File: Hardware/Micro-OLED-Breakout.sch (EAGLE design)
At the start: 23 parts

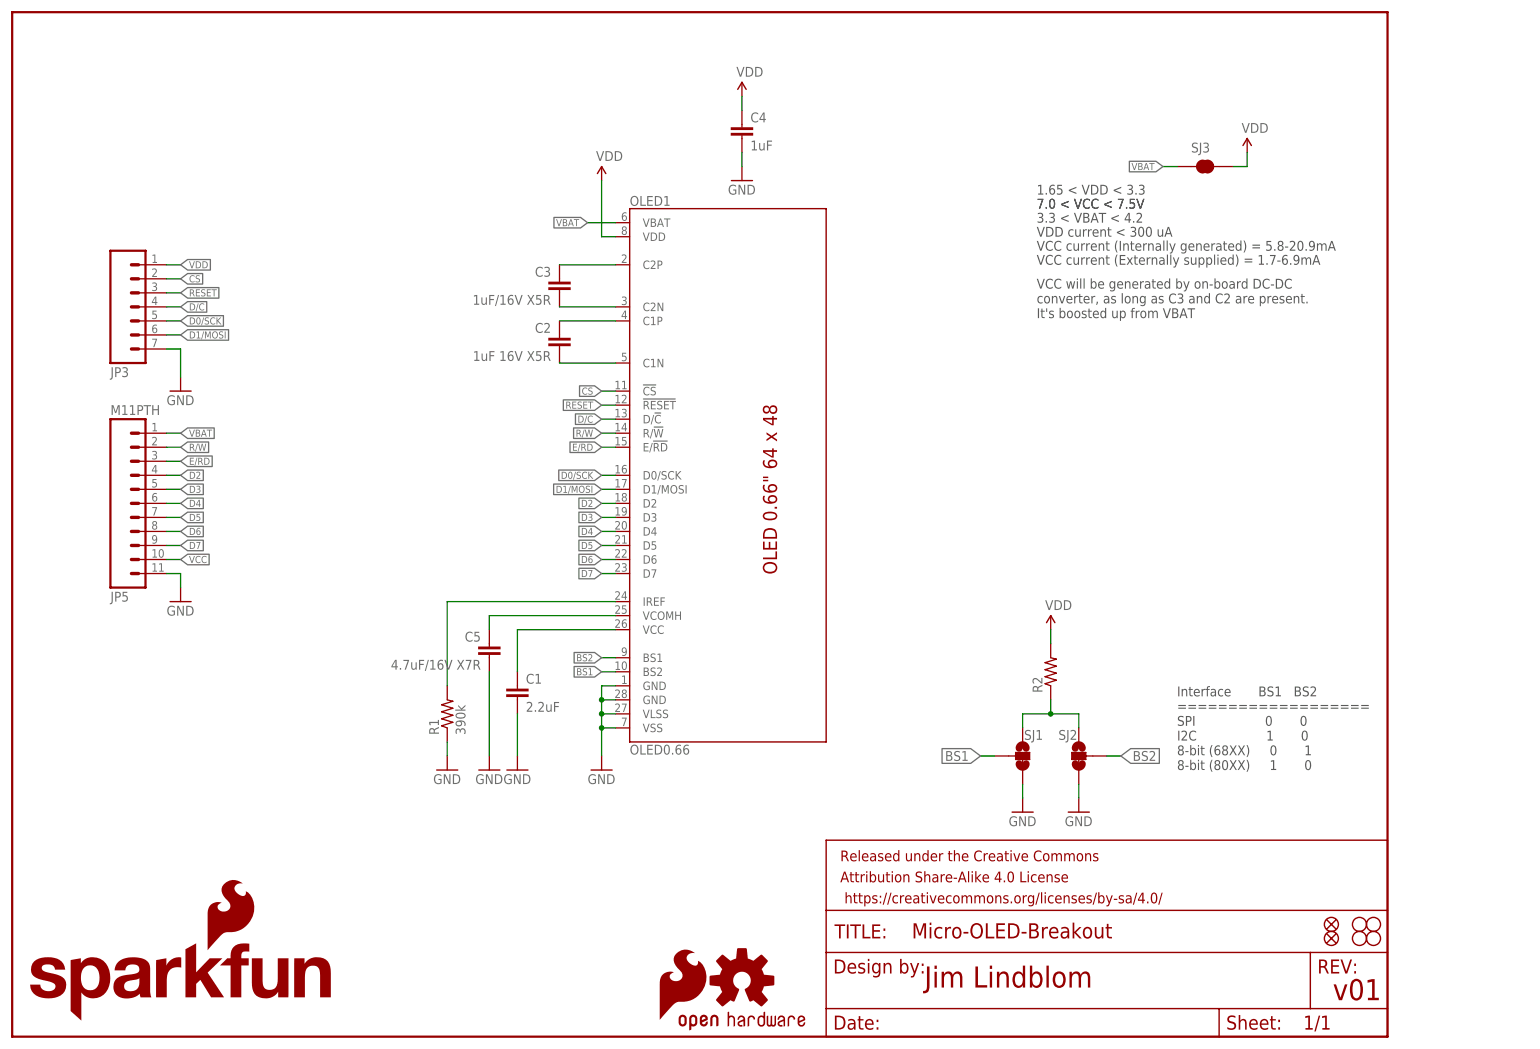
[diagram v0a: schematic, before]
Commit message: Revising board shape, OLED (v02)
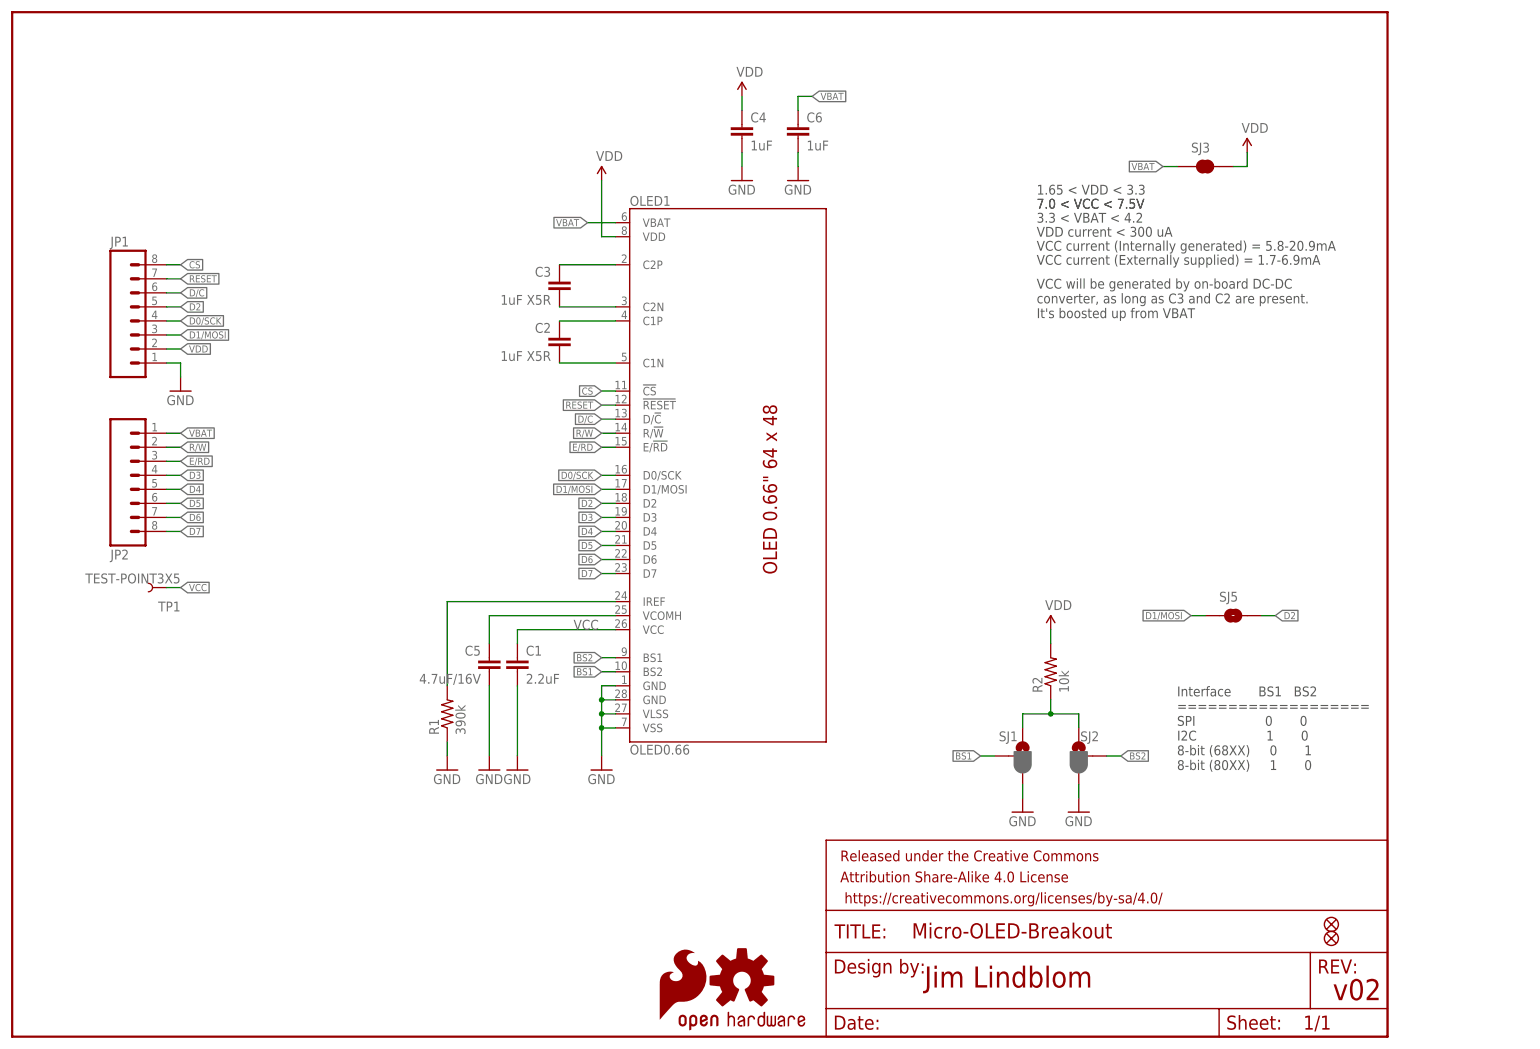
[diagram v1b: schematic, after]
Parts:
- removed JP3: (no value), SparkFun-Connectors:M07
- removed JP5: M11PTH, SparkFun-Connectors:M11PTH
- removed LOGO1: OSHW-LOGOS, SparkFun-Aesthetics:OSHW-LOGOS
- removed STANDOFF1, STANDOFF2, STANDOFF3, STANDOFF4: STAND-OFF, SparkFun-Electromechanical:STAND-OFF
- added C6: 1uF, SparkFun-Passives:CAP0603-CAP
- added JP1, JP2: (no value), SparkFun-Connectors:M08
- added SJ5: JUMPER-PAD-2-NOYES_SILK, SparkFun-Passives:JUMPER-PAD-2-NOYES_SILK
- added TP1: TEST-POINT3X5, SparkFun-Passives:TEST-POINT3X5
- C1: device SparkFun-Passives:CAP0603-CAP -> SparkFun-Passives:CAP0805
- C2: value 1uF 16V X5R -> 1uF X5R; device SparkFun-Passives:CAP0603-CAP -> SparkFun-Passives:CAP0805
- C3: value 1uF/16V X5R -> 1uF X5R; device SparkFun-Passives:CAP0603-CAP -> SparkFun-Passives:CAP0805
- C5: value 4.7uF/16V X7R -> 4.7uF/16V; device SparkFun-Passives:CAP0603-CAP -> SparkFun-Passives:CAP1206
- LOGO3: value SFE_LOGO_NAME_FLAME.1_INCH -> OSHW-LOGOS; device SparkFun-Aesthetics:SFE_LOGO_NAME_FLAME.1_INCH -> SparkFun-Aesthetics:OSHW-LOGOS
- R2: value (none) -> 10k
- SJ1: value JUMPER-PAD-3-2OF3_NC_BY_TRACE -> BS1; device SparkFun-Passives:JUMPER-PAD-3-2OF3_NC_BY_TRACE -> SparkFun-Passives:JUMPER-PAD-3-2OF3_NC_BY_PASTE
- SJ2: value JUMPER-PAD-3-2OF3_NC_BY_TRACE -> BS2; device SparkFun-Passives:JUMPER-PAD-3-2OF3_NC_BY_TRACE -> SparkFun-Passives:JUMPER-PAD-3-2OF3_NC_BY_PASTE
- SJ3: value JUMPER-PAD-2-NC_BY_TRACE -> JUMPER-PAD-2-NC_BY_TRACENO_SILK; device SparkFun-Passives:JUMPER-PAD-2-NC_BY_TRACE -> SparkFun-Passives:JUMPER-PAD-2-NC_BY_TRACENO_SILK
- renumbered LOGO2 to LOGO4
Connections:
- net CS: now also JP1.8; no longer JP3.2
- net D/C: now also JP1.6; no longer JP3.4
- net D0/SCK: now also JP1.4; no longer JP3.5
- net D1/MOSI: now also JP1.3, SJ5.1; no longer JP3.6
- net D2: now also JP1.5, SJ5.2; no longer JP5.4
- net D3: now also JP2.4; no longer JP5.5
- net D4: now also JP2.5; no longer JP5.6
- net D5: now also JP2.6; no longer JP5.7
- net D6: now also JP2.7; no longer JP5.8
- net D7: now also JP2.8; no longer JP5.9
- net E/RD: now also JP2.3; no longer JP5.3
- net GND: now also C6.2, JP1.1; no longer JP3.7, JP5.11
- net R/W: now also JP2.2; no longer JP5.2
- net RESET: now also JP1.7; no longer JP3.3
- net VBAT: now also C6.1, JP2.1; no longer JP5.1
- net VCC: now also TP1.1; no longer JP5.10
- net VDD: now also JP1.2; no longer JP3.1
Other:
- note added: "v02"
- note removed: "v01"
- moved on the sheet: C1, C5

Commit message: Fixing swapped BS1 and BS2 labels (v03)
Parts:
- added TP2: TEST-POINT3X5, SparkFun-Passives:TEST-POINT3X5
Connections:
- net BS1: now also OLED1.BS1; no longer OLED1.BS2
- net BS2: now also OLED1.BS2; no longer OLED1.BS1
- net VCC: now also TP2.1
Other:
- note added: "v03"
- note removed: "v02"

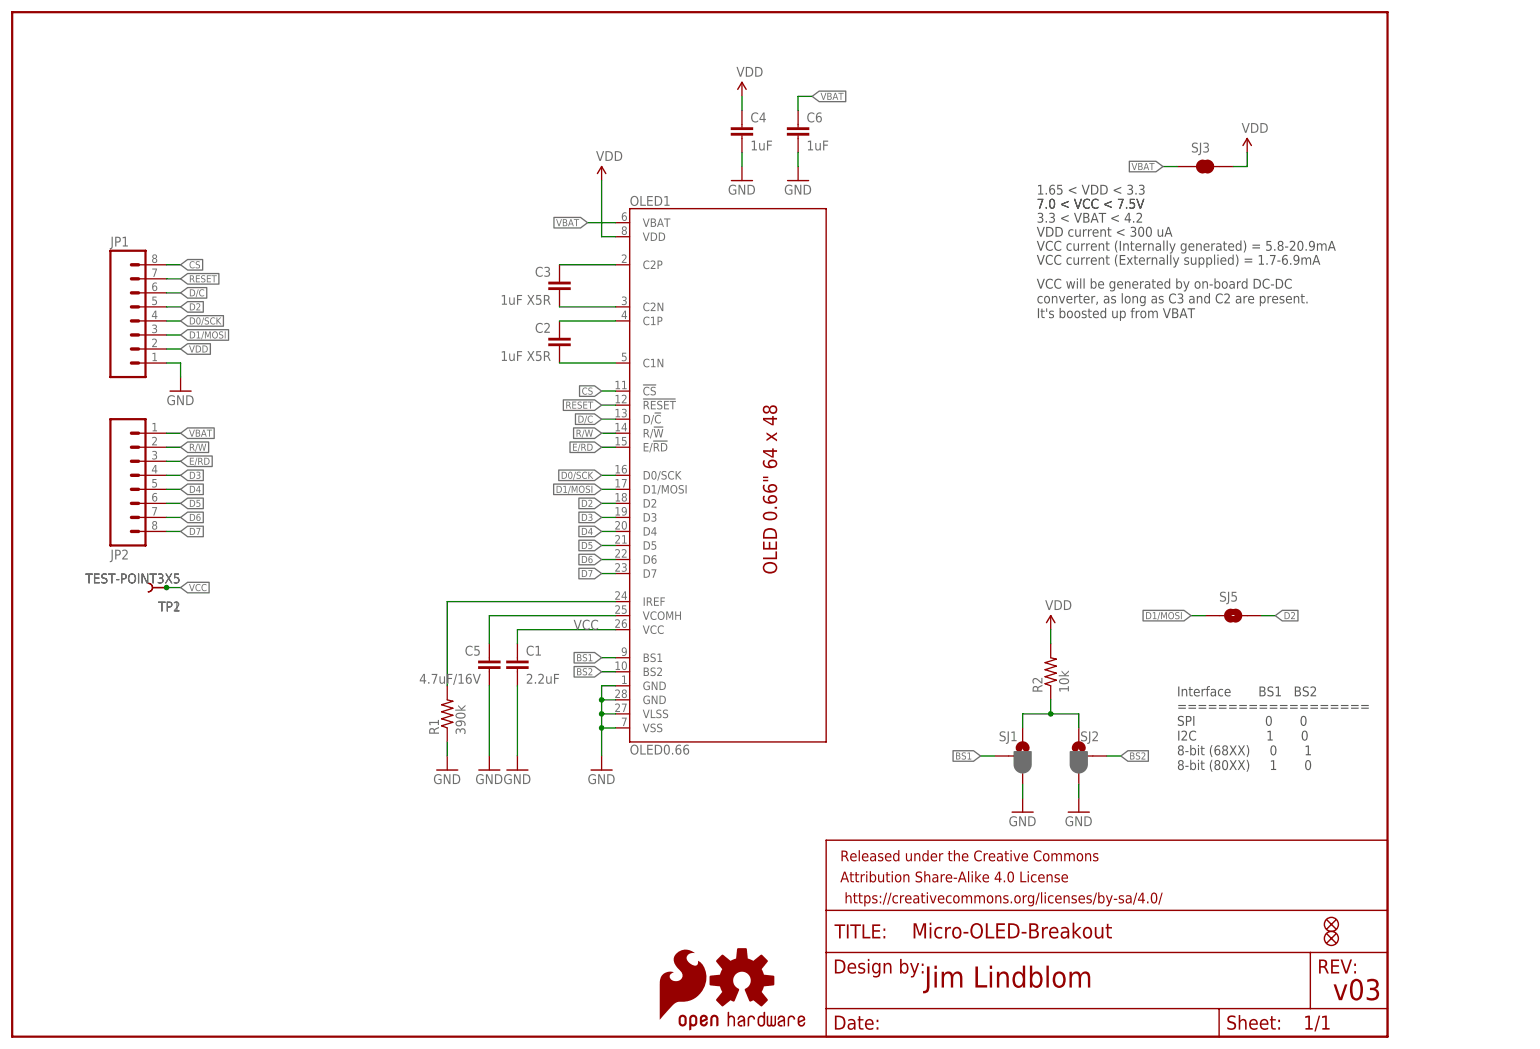
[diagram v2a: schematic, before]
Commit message: Adding D/C jumper (open by default) (v04)
Allows address selection in I2C mode.

Also:
* adding some notes to schematic
* Shuffling around silk labels. Avoiding holes.
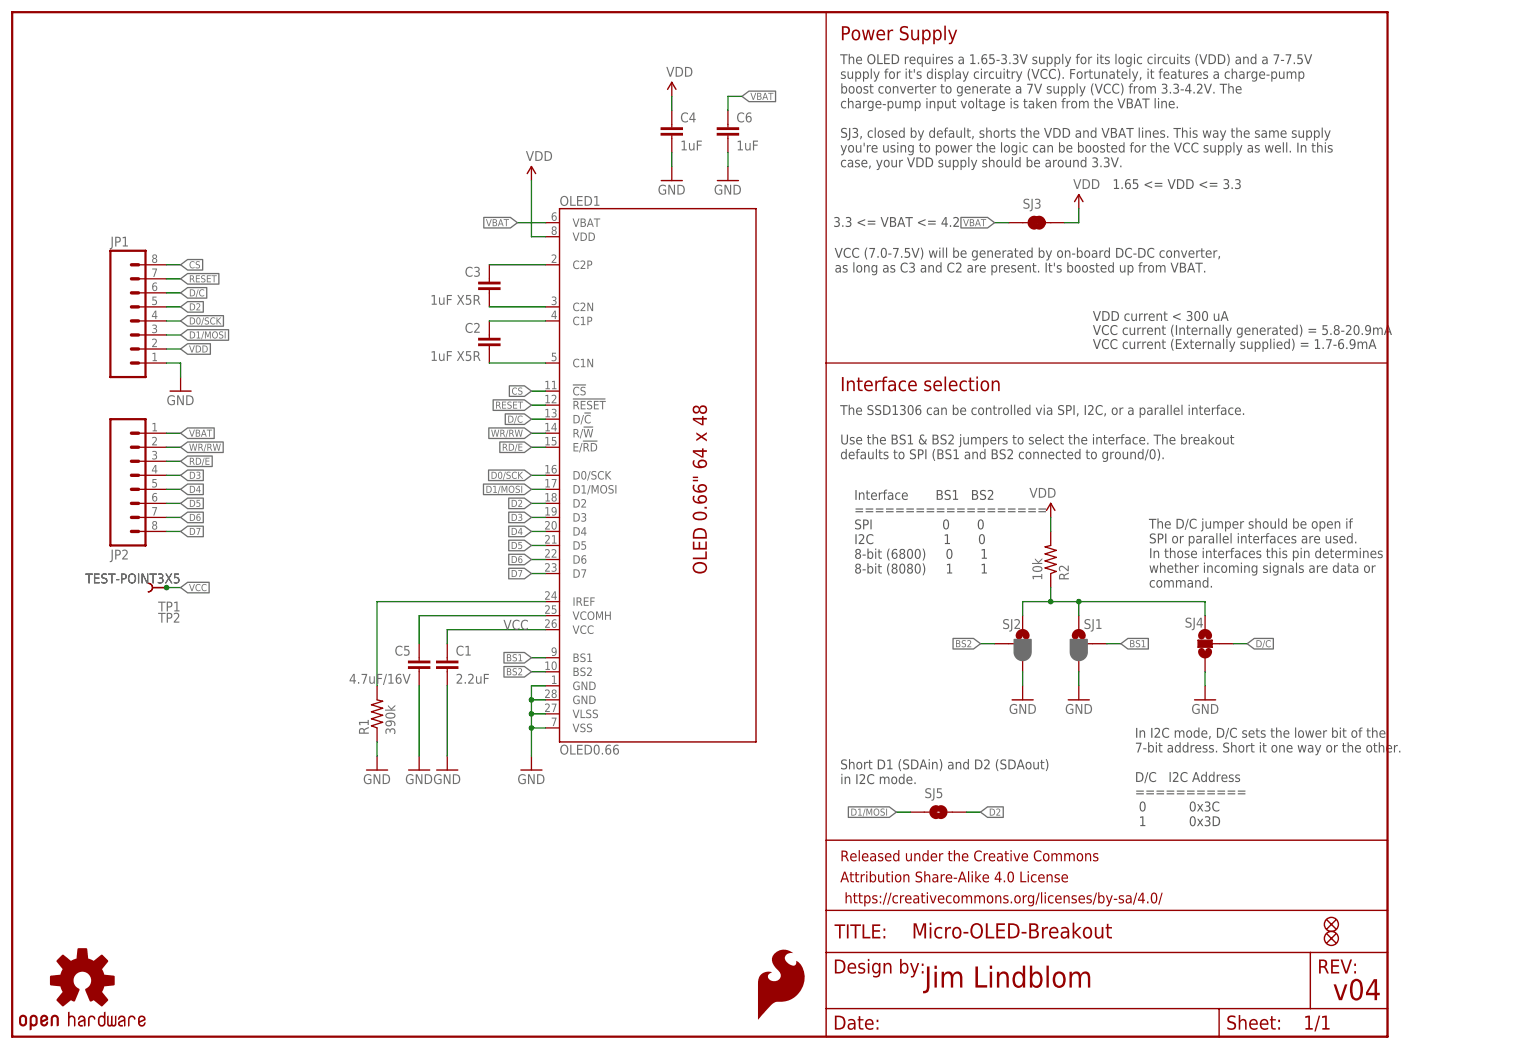
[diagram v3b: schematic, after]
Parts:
- added SJ4: JUMPER-PAD-3-NOTIGHT, SparkFun-Passives:JUMPER-PAD-3-NOTIGHT
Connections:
- net E/RD renamed RD/E
- net R/W renamed WR/RW
- net D/C: now also SJ4.2
- net GND: now also SJ4.3
- net VDD_PU: now also SJ4.1
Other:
- note added: "1.65 <= VDD <= 3.3"
- note added: "3.3 <= VBAT <= 4.2"
- note added: "In I2C mode, D/C sets the lower bit of the 7-bit address. Short it one way or the other. D/C I2C Address =========== 0 0x3C 1 0x3D"
- note added: "Interface BS1 BS2 =================== SPI 0 0 I2C 1 0 8-bit (6800) 0 1 8-bit (8080) 1 1"
- note added: "Interface selection"
- note added: "Power Supply"
- note added: "Short D1 (SDAin) and D2 (SDAout) in I2C mode."
- note added: "The D/C jumper should be open if SPI or parallel interfaces are used. In those interfaces this pin determines whether incoming signals are data or command."
- note added: "The OLED requires a 1.65-3.3V supply for its logic circuits (VDD) and a 7-7.5V supply for it's display circuitry (VCC). Fortunately, it features a charge-pump boost converter to generate a 7V supply (VCC) from 3.3-4.2V. The charge-pump input voltage is taken from the VBAT line. SJ3, closed by default, shorts the VDD and VBAT lines. This way the same supply you're using to power the logic can be b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"
- note added: "The SSD1306 can be controlled via SPI, I2C, or a parallel interface. Use the BS1 & BS2 jumpers to select the interface. The breakout defaults to SPI (BS1 and BS2 connected to ground/0)."
- note added: "VCC (7.0-7.5V) will be generated by on-board DC-DC converter, as long as C3 and C2 are present. It's boosted up from VBAT."
- note added: "v04"
- note removed: "1.65 < VDD < 3.3"
- note removed: "3.3 < VBAT < 4.2"
- note removed: "7.0 < VCC < 7.5V"
- note removed: "Interface BS1 BS2 =================== SPI 0 0 I2C 1 0 8-bit (68XX) 0 1 8-bit (80XX) 1 0"
- note removed: "VCC will be generated by on-board DC-DC converter, as long as C3 and C2 are present. It's boosted up from VBAT"
- note removed: "v03"
- moved on the sheet: C1, C2, C3, C4, C5, C6, OLED1, R1, R2, SJ1, SJ2, SJ3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
